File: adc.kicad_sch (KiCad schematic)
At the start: 13 parts, among them Q801 BSS123, Q802 BSS123, U801 74LS125, U802 MAX11614

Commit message: completed schematic
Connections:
- net +3V3 renamed +3.3V

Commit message: majority of layout done
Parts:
- U801: footprint Package_SO:SOIC-16_3.9x9.9mm_P1.27mm -> Package_SO:SOIC-14_3.9x8.7mm_P1.27mm
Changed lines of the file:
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@@
       (effects (font (size 1.27 1.27)))
     )
-    (property "Footprint" "Package_SO:SOIC-16_3.9x9.9mm_P1.27mm" (at 196.85 107.95 0)
+    (property "Footprint" "Package_SO:SOIC-14_3.9x8.7mm_P1.27mm" (at 196.85 107.95 0)
       (effects (font (size 1.27 1.27)) hide)
     )
@@
       (effects (font (size 1.27 1.27)))
     )
-    (property "Footprint" "Package_SO:SOIC-16_3.9x9.9mm_P1.27mm" (at 196.85 76.2 0)
+    (property "Footprint" "Package_SO:SOIC-14_3.9x8.7mm_P1.27mm" (at 196.85 76.2 0)
       (effects (font (size 1.27 1.27)) hide)
     )
@@
       (effects (font (size 1.27 1.27)))
     )
-    (property "Footprint" "Package_SO:SOIC-16_3.9x9.9mm_P1.27mm" (at 196.85 139.7 0)
+    (property "Footprint" "Package_SO:SOIC-14_3.9x8.7mm_P1.27mm" (at 196.85 139.7 0)
       (effects (font (size 1.27 1.27)) hide)
     )
@@
       (effects (font (size 1.27 1.27)) (justify left))
     )
-    (property "Footprint" "Package_SO:SOIC-16_3.9x9.9mm_P1.27mm" (at 139.7 171.45 0)
+    (property "Footprint" "Package_SO:SOIC-14_3.9x8.7mm_P1.27mm" (at 139.7 171.45 0)
       (effects (font (size 1.27 1.27)) hide)
     )
@@
       (effects (font (size 1.27 1.27)))
     )
-    (property "Footprint" "Package_SO:SOIC-16_3.9x9.9mm_P1.27mm" (at 196.85 44.45 0)
-      (effects (font (size 1.27 1.27)) hide)
-    )
+    (property "Footprint" "Package_SO:SOIC-14_3.9x8.7mm_P1.27mm" (at 196.85 44.45 0)
+      (effects (font (size 1.27 1.27)) hide)
+    )

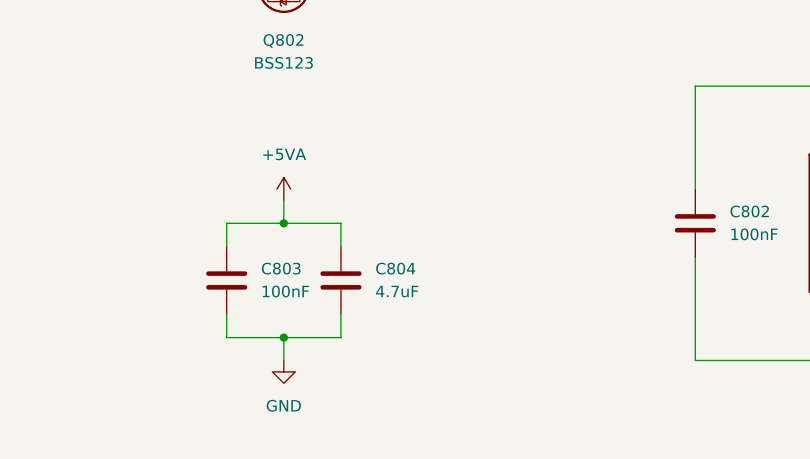
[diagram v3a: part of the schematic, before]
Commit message: fixed oscillator and component values
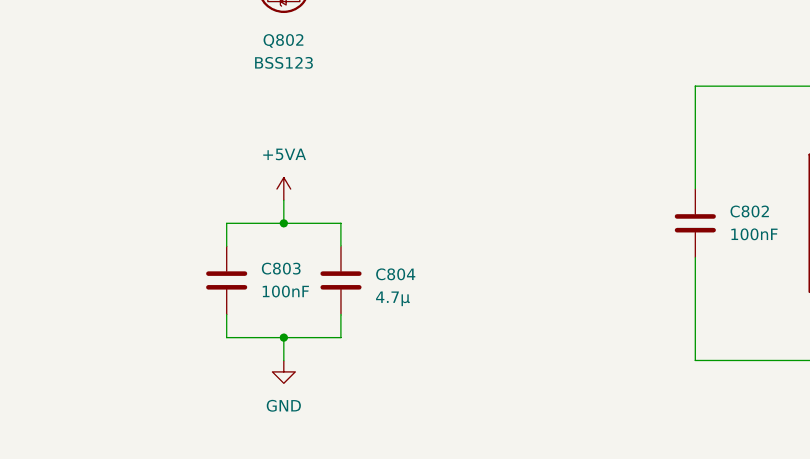
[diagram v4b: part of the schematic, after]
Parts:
- C804: value 4.7uF -> 4.7µ; footprint Capacitor_SMD:C_0805_2012Metric -> Capacitor_SMD:C_0603_1608Metric
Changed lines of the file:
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@@
   (symbol (lib_id "Device:C") (at 82.55 177.8 0) (unit 1)
     (in_bom yes) (on_board yes) (dnp no) (fields_autoplaced)
-    (property "Reference" "C804" (at 86.36 176.5299 0)
+    (property "Reference" "C804" (at 86.36 177.165 0)
       (effects (font (size 1.27 1.27)) (justify left))
     )
-    (property "Value" "4.7uF" (at 86.36 179.0699 0)
+    (property "Value" "4.7µ" (at 86.36 179.705 0)
       (effects (font (size 1.27 1.27)) (justify left))
     )
-    (property "Footprint" "Capacitor_SMD:C_0805_2012Metric" (at 83.5152 181.61 0)
+    (property "Footprint" "Capacitor_SMD:C_0603_1608Metric" (at 83.5152 181.61 0)
       (effects (font (size 1.27 1.27)) hide)
     )

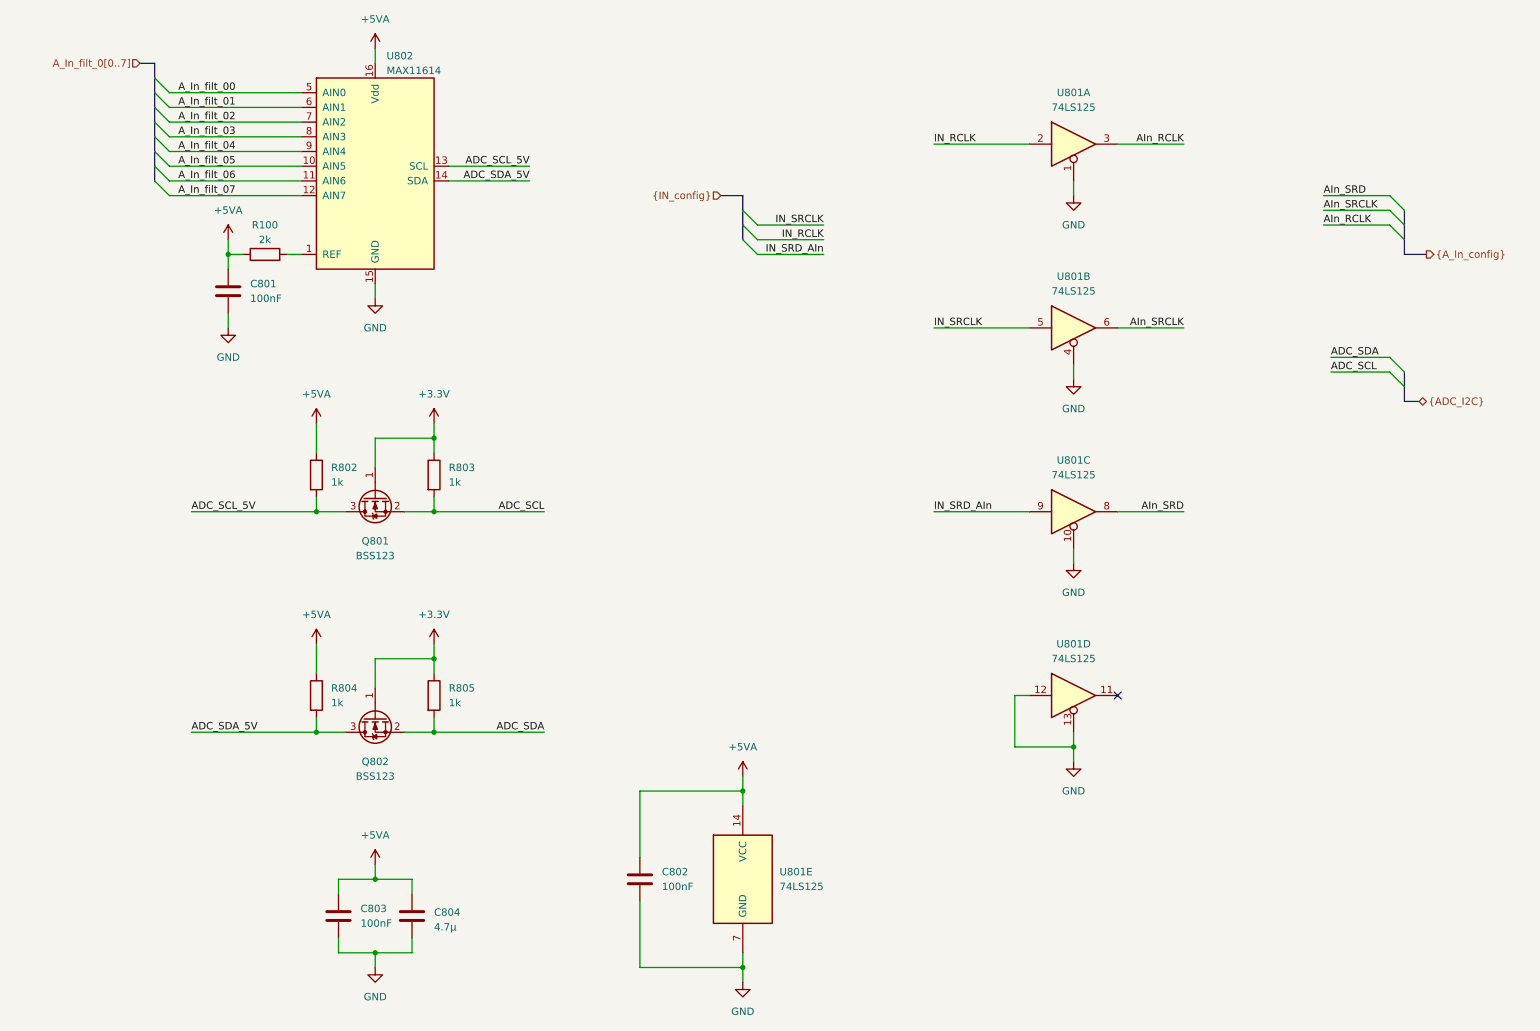
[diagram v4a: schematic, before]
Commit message: hierarchical sheets for digital I/O and replaced power supply jumpers with relays
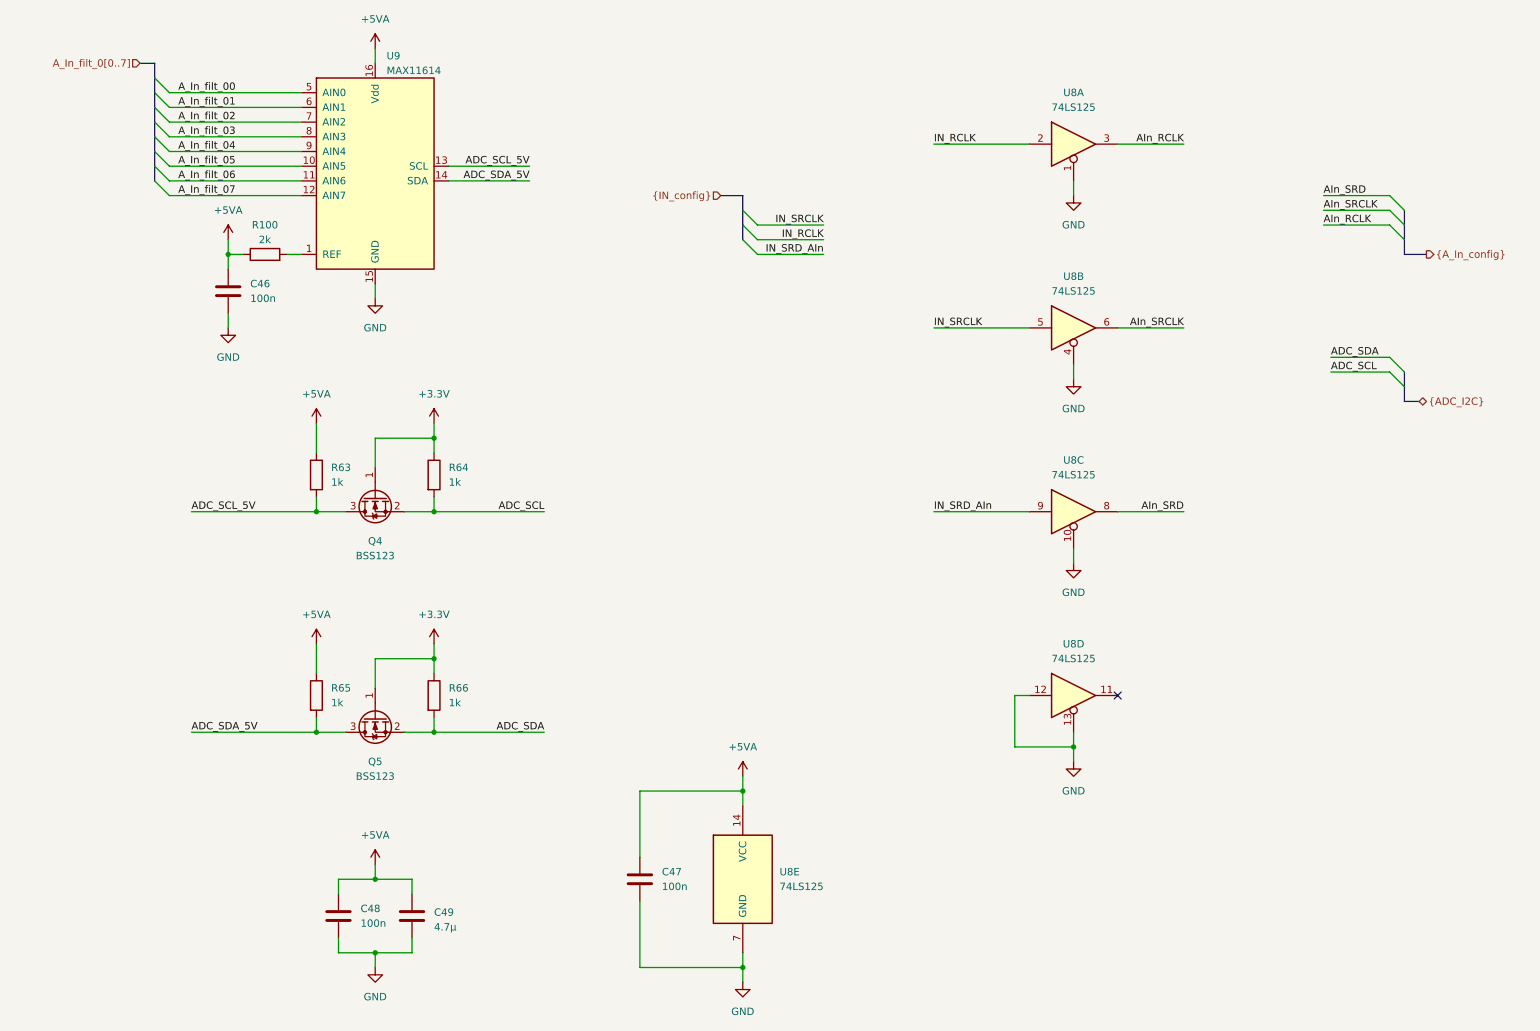
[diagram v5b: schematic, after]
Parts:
- C46: renamed from C801; value 100nF -> 100n
- C47: renamed from C802; value 100nF -> 100n
- C48: renamed from C803; value 100nF -> 100n
- renumbered C804 to C49, Q801 to Q4, Q802 to Q5, R802 to R63, R803 to R64, R804 to R65, R805 to R66, U801 to U8, U802 to U9
